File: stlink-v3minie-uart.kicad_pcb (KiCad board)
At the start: 2 copper layers, 14 x 23 mm, 3 parts, among them J1 Conn_01x05, J2 Conn_02x05_Top_Bottom, J3 Conn_01x04_Pin

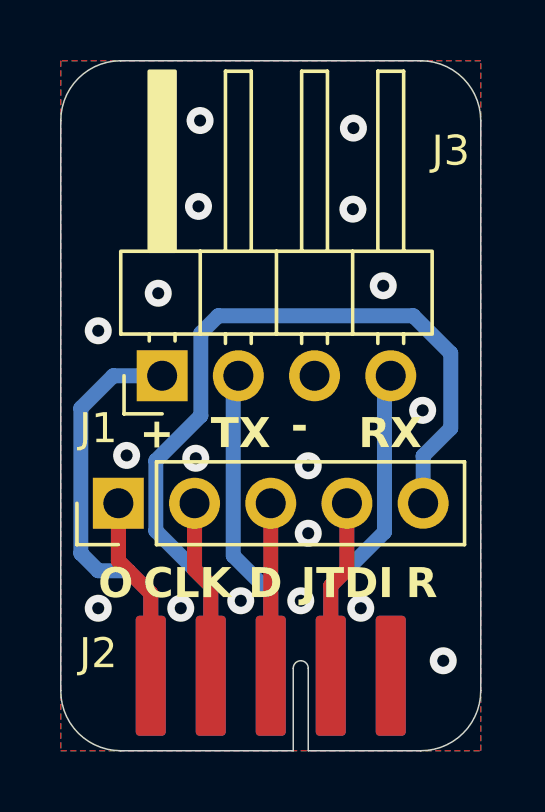
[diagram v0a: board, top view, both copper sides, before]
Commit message: schem/pcb: fix pin numbering
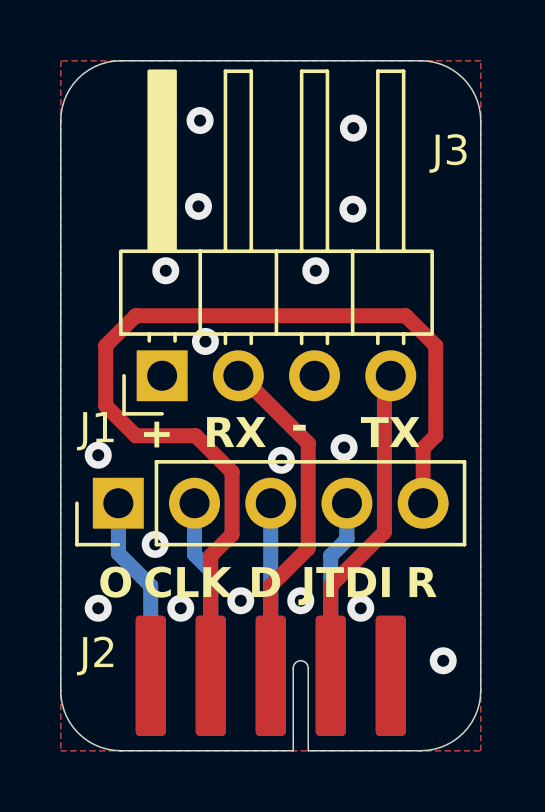
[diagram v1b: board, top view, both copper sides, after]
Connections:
- J2 pad 1: unconnected-(J2-Pin_1-Pad1) -> GND
- J2 pad 10: +3V3 -> /SWO
- J2 pad 2: /JTDI -> /VCP_RX
- J2 pad 3: /SWDIO -> /VCP_TX
- J2 pad 4: /SWCLK -> /nRST
- J2 pad 5: /SWO -> +3V3
- J2 pad 6: GND -> unconnected-(J2-Pin_6-Pad6)
- J2 pad 7: /VCP_RX -> /JTDI
- J2 pad 8: /VCP_TX -> /SWDIO
- J2 pad 9: /nRST -> /SWCLK
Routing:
- net +3V3: track 13.6 -> 0.00 mm
- net /nRST: track 27.3 -> 31.5 mm
- net /VCP_TX: track 10.6 -> 11.5 mm
- net GND: vias 18 -> 17

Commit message: rev 02
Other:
- board text added: "R02"
- board text removed: "R01"
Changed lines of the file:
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@@
 		(title "STLINK-V3 MINIE UART")
 		(date "2026-05-26")
-		(rev "01")
+		(rev "02")
 		(company "Rémi Ait-Younes")
 	)
@@
 		)
 	)
-	(gr_text "R01"
+	(gr_text "R02"
 		(at 146.361734 98.916522 0)
 		(layer "B.SilkS")

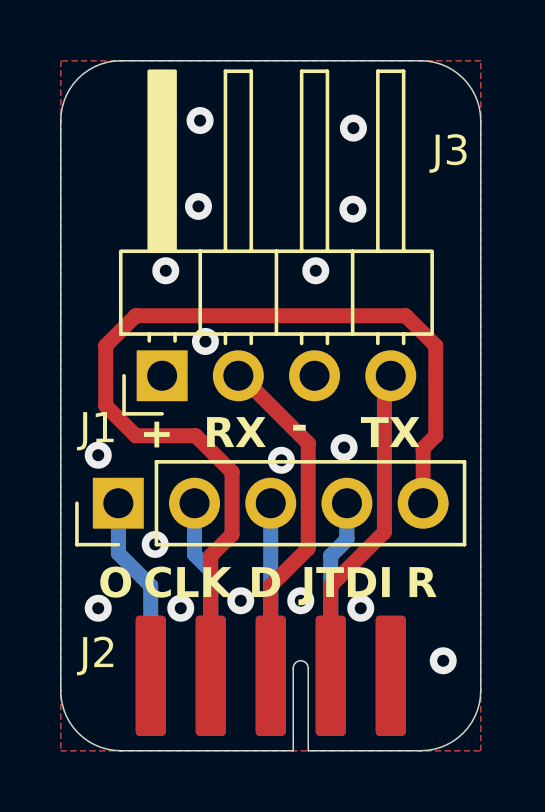
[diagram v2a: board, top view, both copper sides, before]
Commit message: pcb: add missing track
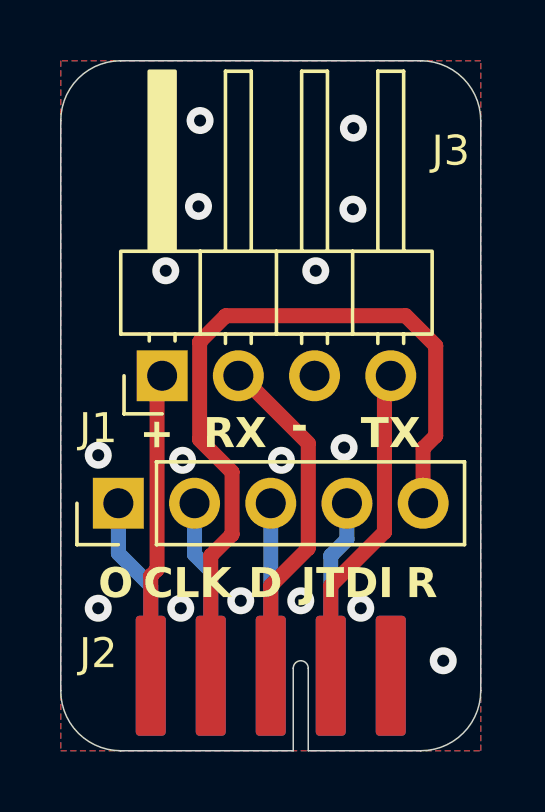
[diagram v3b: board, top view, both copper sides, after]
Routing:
- net +3V3: track 0.00 -> 10.2 mm
- net /nRST: track 31.5 -> 25.9 mm
- net GND: vias 17 -> 16
